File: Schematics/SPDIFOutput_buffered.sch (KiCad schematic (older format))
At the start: 4 parts, among them U5 74HC04

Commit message: Updated PCB design
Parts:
- R6: footprint Resistor_THT:R_Axial_DIN0207_L6.3mm_D2.5mm_P10.16mm_Horizontal -> Resistor_THT:R_Axial_DIN0207_L6.3mm_D2.5mm_P5.08mm_Vertical
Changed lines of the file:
@@
 EESchema Schematic File Version 4
 LIBS:RenaultBT-cache
-EELAYER 26 0
+EELAYER 29 0
 EELAYER END
 $Descr A4 11693 8268
@@
 F 0 "R6" H 7870 4096 50  0000 L CNN
 F 1 "93" H 7870 4005 50  0000 L CNN
-F 2 "Resistor_THT:R_Axial_DIN0207_L6.3mm_D2.5mm_P10.16mm_Horizontal" V 7730 4050 50  0001 C CNN
+F 2 "Resistor_THT:R_Axial_DIN0207_L6.3mm_D2.5mm_P5.08mm_Vertical" V 7730 4050 50  0001 C CNN
 F 3 "~" H 7800 4050 50  0001 C CNN
 	1    7800 4050

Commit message: Modified PCB design
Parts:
- R5: footprint Resistor_THT:R_Axial_DIN0207_L6.3mm_D2.5mm_P10.16mm_Horizontal -> Resistor_THT:R_Axial_DIN0207_L6.3mm_D2.5mm_P7.62mm_Horizontal
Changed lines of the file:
@@
 EESchema Schematic File Version 4
 LIBS:RenaultBT-cache
-EELAYER 29 0
+EELAYER 26 0
 EELAYER END
 $Descr A4 11693 8268
@@
 F 0 "R5" V 7143 3650 50  0000 C CNN
 F 1 "374" V 7234 3650 50  0000 C CNN
-F 2 "Resistor_THT:R_Axial_DIN0207_L6.3mm_D2.5mm_P10.16mm_Horizontal" V 7280 3650 50  0001 C CNN
+F 2 "Resistor_THT:R_Axial_DIN0207_L6.3mm_D2.5mm_P7.62mm_Horizontal" V 7280 3650 50  0001 C CNN
 F 3 "~" H 7350 3650 50  0001 C CNN
 	1    7350 3650

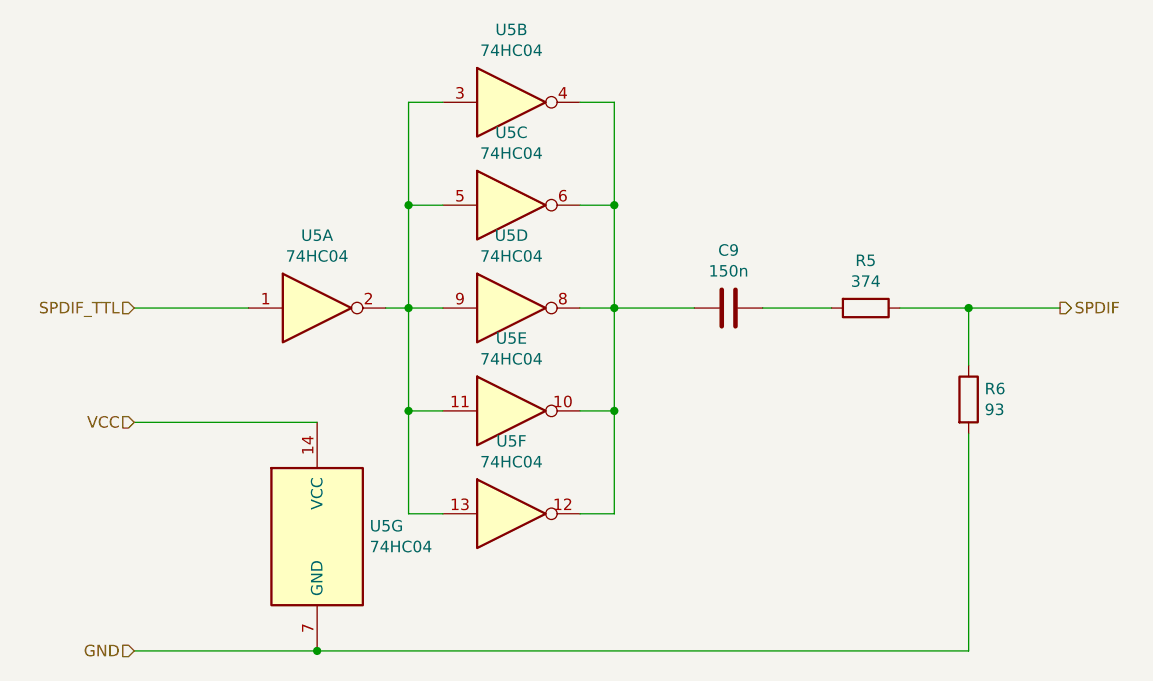
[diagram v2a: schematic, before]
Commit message: Fixed CDC interface schematic; Fixed SPDIF output interface schematic; Added screw terminals; Modified PCB design
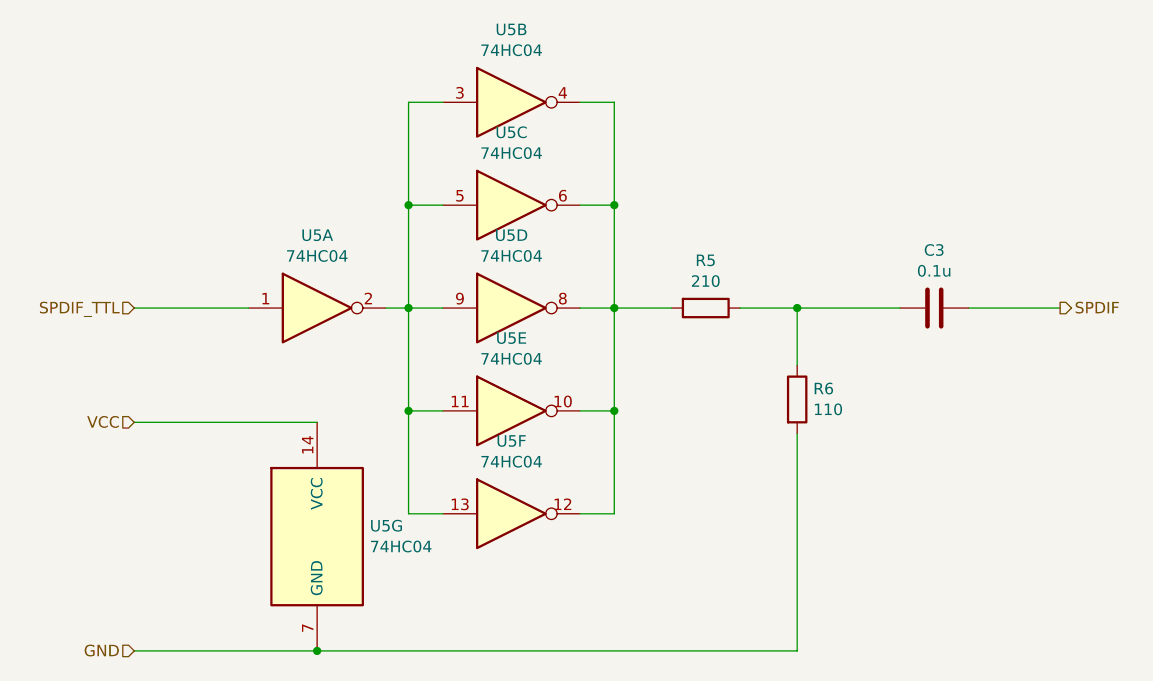
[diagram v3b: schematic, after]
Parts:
- removed C9: 150n, Capacitor_THT:C_Disc_D5.0mm_W2.5mm_P2.50mm, symbol Device:C
- added C3: 0.1u, Capacitor_THT:C_Disc_D5.0mm_W2.5mm_P2.50mm, symbol Device:C
- R5: value 374 -> 210; footprint Resistor_THT:R_Axial_DIN0207_L6.3mm_D2.5mm_P7.62mm_Horizontal -> Resistor_THT:R_Axial_DIN0207_L6.3mm_D2.5mm_P10.16mm_Horizontal
- R6: value 93 -> 110; footprint Resistor_THT:R_Axial_DIN0207_L6.3mm_D2.5mm_P5.08mm_Vertical -> Resistor_THT:R_Axial_DIN0207_L6.3mm_D2.5mm_P10.16mm_Horizontal
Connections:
- net SPDIF: now also C3.1; no longer R5.1, R6.1
- net at U5.10, U5.12, U5.4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: now also R5.2
- new net: C3.2, R5.1, R6.1
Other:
- moved on the sheet: R5, R6
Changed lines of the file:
@@
 GND
-$Comp
-L Device:C C9
-U 1 1 5CD2DB1E
-P 6750 3650
-F 0 "C9" V 6498 3650 50  0000 C CNN
-F 1 "150n" V 6589 3650 50  0000 C CNN
-F 2 "Capacitor_THT:C_Disc_D5.0mm_W2.5mm_P2.50mm" H 6788 3500 50  0001 C CNN
-F 3 "~" H 6750 3650 50  0001 C CNN
-	1    6750 3650
-	0    1    1    0
-$EndComp
 $Comp
 L Device:R R5
 U 1 1 5CD2DB92
-P 7350 3650
-F 0 "R5" V 7143 3650 50  0000 C CNN
-F 1 "374" V 7234 3650 50  0000 C CNN
-F 2 "Resistor_THT:R_Axial_DIN0207_L6.3mm_D2.5mm_P7.62mm_Horizontal" V 7280 3650 50  0001 C CNN
-F 3 "~" H 7350 3650 50  0001 C CNN
-	1    7350 3650
+P 6650 3650
+F 0 "R5" V 6443 3650 50  0000 C CNN
+F 1 "210" V 6534 3650 50  0000 C CNN
+F 2 "Resistor_THT:R_Axial_DIN0207_L6.3mm_D2.5mm_P10.16mm_Horizontal" V 6580 3650 50  0001 C CNN
+F 3 "~" H 6650 3650 50  0001 C CNN
+	1    6650 3650
 	0    1    1    0
 $EndComp
@@
 L Device:R R6
 U 1 1 5CD2DBF9
-P 7800 4050
-F 0 "R6" H 7870 4096 50  0000 L CNN
-F 1 "93" H 7870 4005 50  0000 L CNN
-F 2 "Resistor_THT:R_Axial_DIN0207_L6.3mm_D2.5mm_P5.08mm_Vertical" V 7730 4050 50  0001 C CNN
-F 3 "~" H 7800 4050 50  0001 C CNN
-	1    7800 4050
+P 7050 4050
+F 0 "R6" H 7120 4096 50  0000 L CNN
+F 1 "110" H 7120 4005 50  0000 L CNN
+F 2 "Resistor_THT:R_Axial_DIN0207_L6.3mm_D2.5mm_P10.16mm_Horizontal" V 6980 4050 50  0001 C CNN
+F 3 "~" H 7050 4050 50  0001 C CNN
+	1    7050 4050
 	1    0    0    -1
 $EndComp
@@
 SPDIF
 Wire Wire Line
-	6250 3650 6600 3650
-Wire Wire Line
-	6900 3650 7200 3650
-Wire Wire Line
-	7500 3650 7800 3650
-Wire Wire Line
-	7800 3900 7800 3650
-Connection ~ 7800 3650
-Wire Wire Line
 	7800 3650 8200 3650
 Wire Wire Line
-	4950 5150 7800 5150
-Wire Wire Line
-	7800 5150 7800 4200
+	4950 5150 7050 5150
 Connection ~ 4950 5150
 Wire Wire Line
@@
 Wire Wire Line
 	4150 3650 4650 3650
+$Comp
+L Device:C C3
+U 1 1 5D46DA2E
+P 7650 3650
+F 0 "C3" V 7398 3650 50  0000 C CNN
+F 1 "0.1u" V 7489 3650 50  0000 C CNN
+F 2 "Capacitor_THT:C_Disc_D5.0mm_W2.5mm_P2.50mm" H 7688 3500 50  0001 C CNN
+F 3 "~" H 7650 3650 50  0001 C CNN
+	1    7650 3650
+	0    1    1    0
+$EndComp
+Wire Wire Line
+	6250 3650 6500 3650
+Wire Wire Line
+	6800 3650 7050 3650
+Wire Wire Line
+	7050 3900 7050 3650
+Connection ~ 7050 3650
+Wire Wire Line
+	7050 3650 7500 3650
+Wire Wire Line
+	7050 4200 7050 5150
 $EndSCHEMATC
